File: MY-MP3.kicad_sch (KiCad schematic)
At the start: 62 parts, among them J1 microSD, J2 USB_C_Receptacle, J3 JST_2mm_LiPo, J4 Adafruit 5393 Headers, J5 Adafruit 5394 Headers, J6 Newxie Headers, J7 AudioJack4_Ground, Q1 DMG3415U, SW1 SMD_6x3.5mm_h2.5mm, U1 STM32L4R5VITx, U2 CODECODER-VS1053B_LQFP48_, U4 MAX17048, U6 MCP73831-2-OT, U7 AP7312-1833W6, Y1 ABM3-12.288MHZ-D2Y-T, Y2 8 mHz

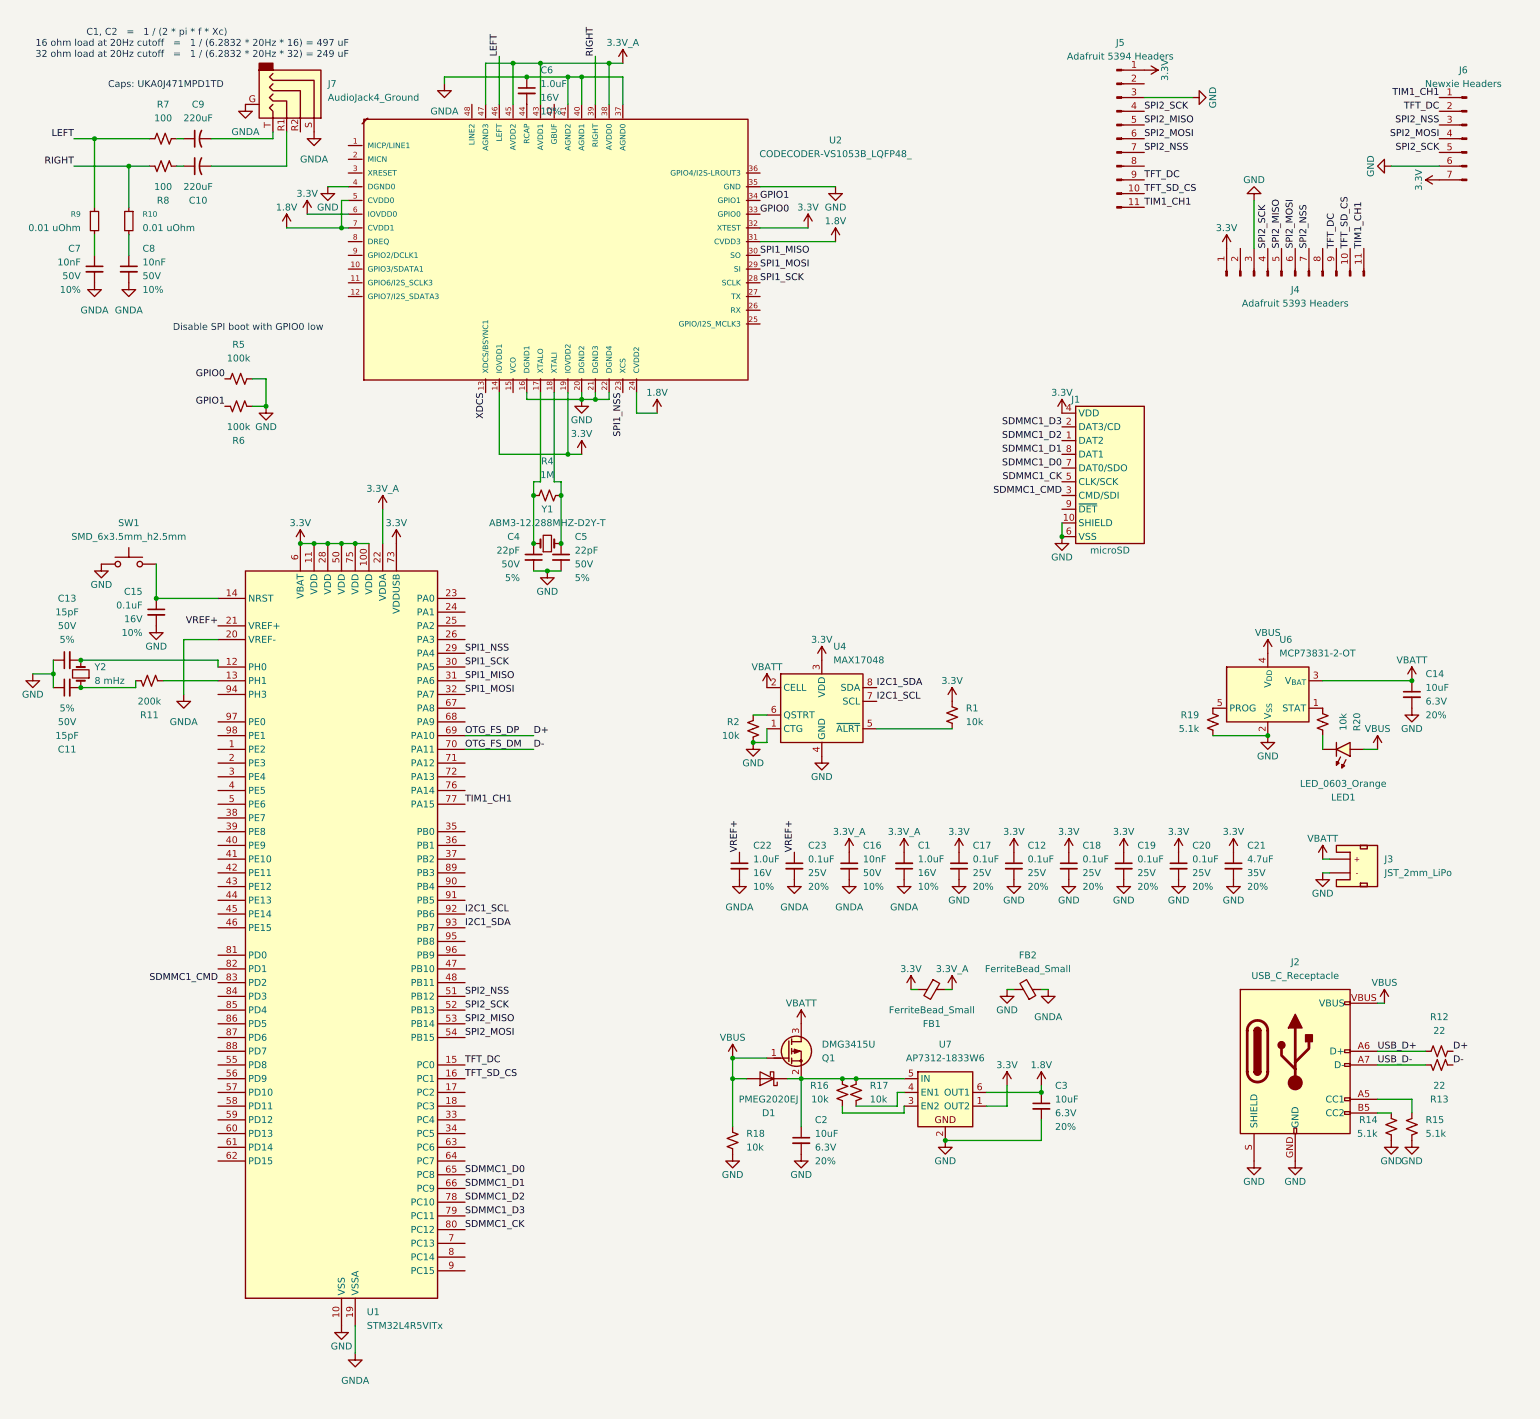
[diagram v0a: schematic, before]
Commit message: Added some buttons and started the on off hardware functionallity
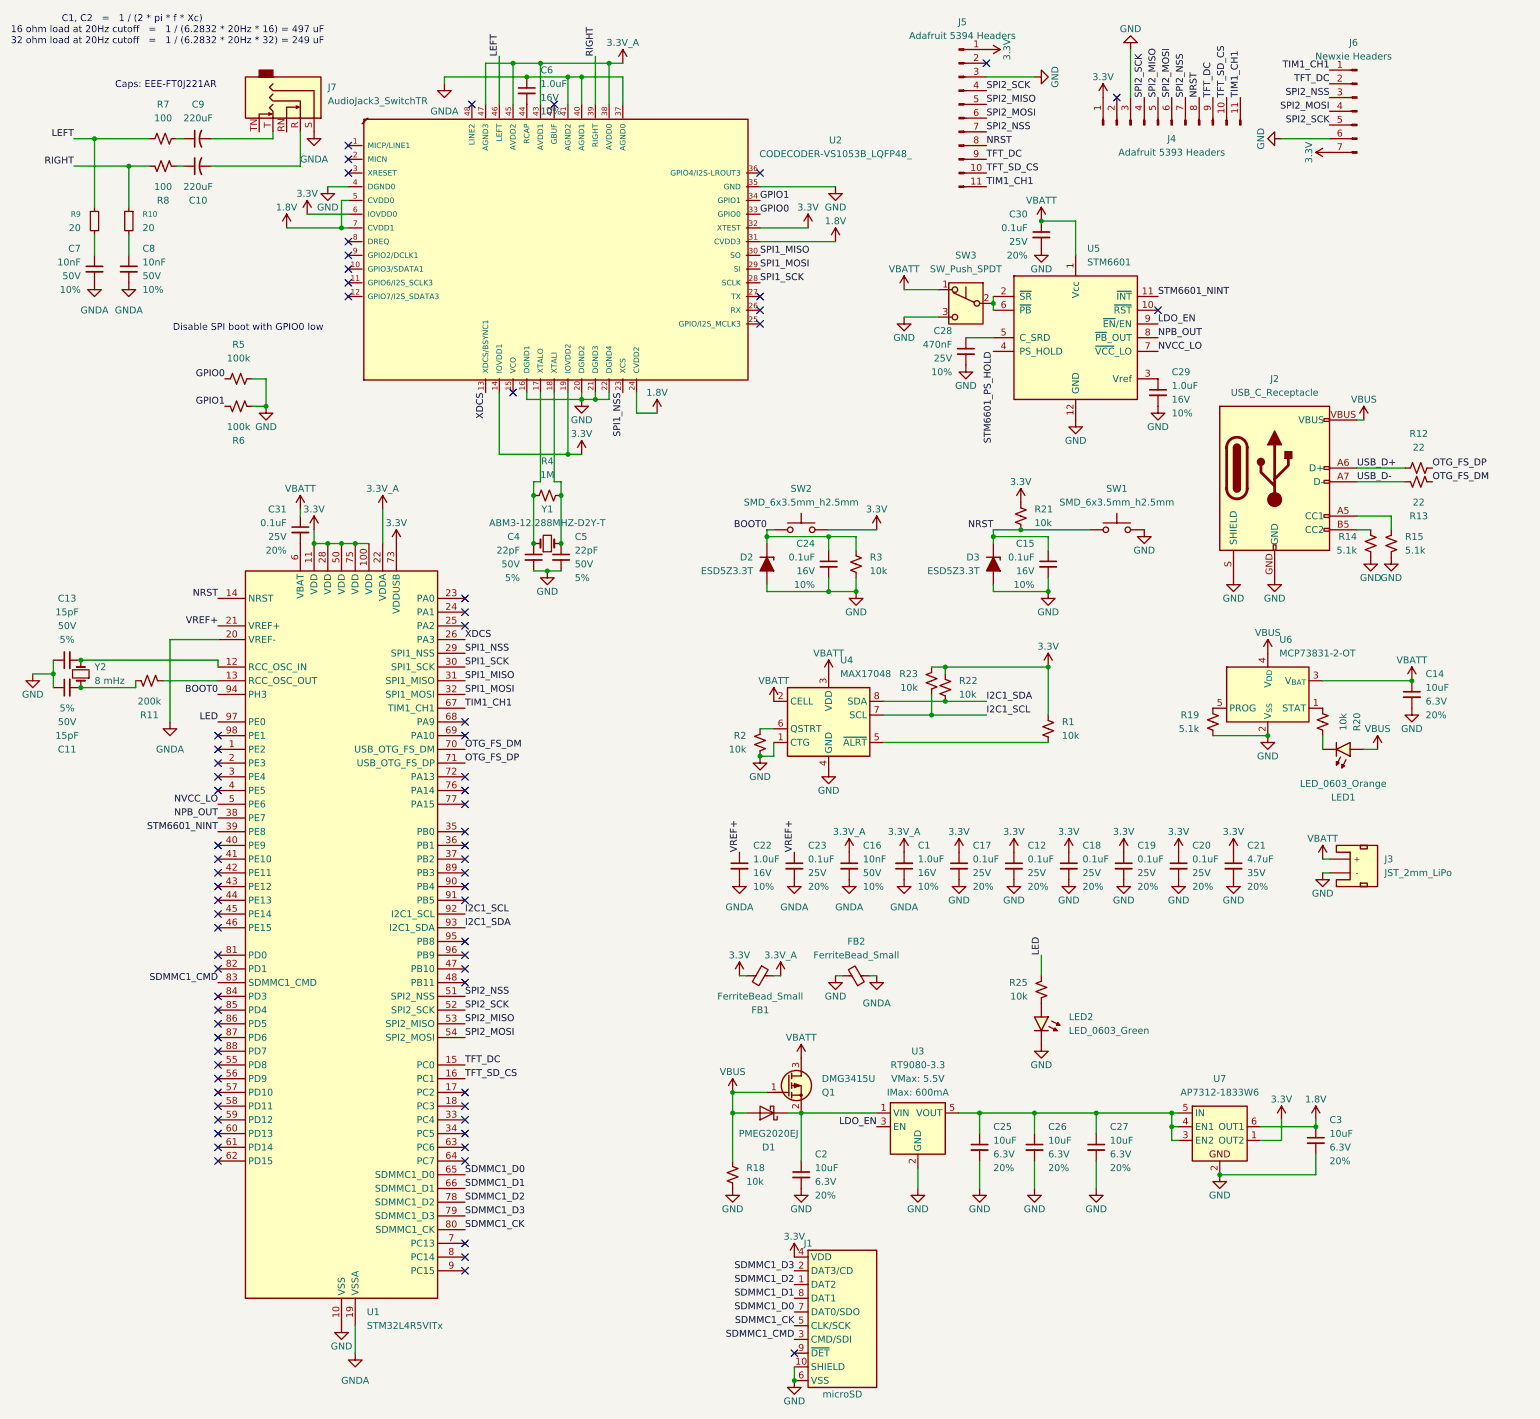
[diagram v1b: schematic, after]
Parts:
- removed J7: AudioJack4_Ground, Connector_Audio:Jack_3.5mm_CUI_SJ1-3525N_Horizontal, symbol Connector_Audio:AudioJack4_Ground
- removed R16, R17: 10k, PCM_SparkFun-Resistor:R_0603_1608Metric, symbol PCM_SparkFun-Resistor:10k_0603
- added C24: 0.1uF, PCM_SparkFun-Capacitor:C_0402_1005Metric, symbol PCM_SparkFun-Capacitor:0.1uF_0402_16V_10%
- added C25, C26, C27: 10uF, PCM_SparkFun-Capacitor:C_0603_1608Metric, symbol PCM_SparkFun-Capacitor:10uF_0603_6.3V_20%
- added C28: 470nF, PCM_SparkFun-Capacitor:C_0402_1005Metric, symbol PCM_SparkFun-Capacitor:470nF_0402_25V_10%
- added C29: 1.0uF, PCM_SparkFun-Capacitor:C_0603_1608Metric, symbol PCM_SparkFun-Capacitor:1.0uF_0603_16V_10%
- added C30, C31: 0.1uF, PCM_SparkFun-Capacitor:C_0603_1608Metric, symbol PCM_SparkFun-Capacitor:0.1uF_0603_25V_20%
- added D2, D3: ESD5Z3.3T, PCM_Diode_SMD_AKL:D_SOD-523, symbol PCM_Diode_TVS_AKL:ESD5Z3.3T
- added J7: AudioJack3_SwitchTR, Connector_Audio:Jack_3.5mm_CUI_SJ1-3525N_Horizontal, symbol Connector_Audio:AudioJack3_SwitchTR
- added LED2: LED_0603_Green, PCM_LED_SMD_AKL:LED_0603_1608Metric, symbol PCM_LED_AKL:LED_0603_Green
- added R21, R25, R3: 10k, PCM_SparkFun-Resistor:R_0603_1608Metric, symbol PCM_SparkFun-Resistor:10k_0603
- added R22, R23: 10k, PCM_SparkFun-Resistor:R_0402_1005Metric, symbol PCM_SparkFun-Resistor:10k_0402
- added SW2: SMD_6x3.5mm_h2.5mm, PCM_SparkFun-Switch:Push_SMD_6x3.5mm, symbol PCM_SparkFun-Switch:SPST_Push_SMD_6x3.5mm_h2.5mm
- added SW3: SW_Push_SPDT, symbol Switch:SW_Push_SPDT
- added U3: RT9080-3.3, PCM_SparkFun-Semiconductor-Standard:SOT23-5, symbol PCM_SparkFun-Regulator:RT9080-3.3
- added U5: STM6601, Package_DFN_QFN:TDFN-12_2x3mm_P0.5mm, symbol Power_Management:STM6601
- C10, C9: footprint (none) -> Capacitor_SMD:CP_Elec_5x5.8
- R10, R9: value 0.01 uOhm -> 20; footprint (none) -> Resistor_SMD:R_0201_0603Metric_Pad0.64x0.40mm_HandSolder
- U2: footprint CODECODER-VS1053B_LQFP48_:LQFP48-0.5-7X7MM -> Package_QFP:LQFP-48_7x7mm_P0.5mm
- Y2: footprint PCM_SparkFun-Clock:Crystal-SMD-5x3.2mm -> Crystal:Crystal_SMD_Abracon_ABM3-2Pin_5.0x3.2mm_HandSoldering
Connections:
- net 3.3V: now also R21.1, R22.2, R23.2, SW2.1; no longer U1.6 (VBAT), U4.3 (VDD)
- net GND: now also SW1.2, C24.2, C25.2, C26.2, C27.2, C28.2, C29.2, C30.2, D2.2 (A), D3.2 (A), LED2.1 (K), R3.2, SW3.3 (C), U3.2 (GND), U5.12 (GND); no longer SW1.1
- net GNDA: now also J7.S
- net I2C1_SCL: now also R23.1
- net I2C1_SDA: now also R22.1
- net TIM1_CH1: now also U1.67 (PA8); no longer U1.77 (PA15)
- net VBATT: now also U4.3 (VDD), C30.1, C31.1, SW3.1 (A), U5.1 (Vcc)
- net XDCS: now also U1.26 (PA3)
- net at C10.2: now also J7.R
- net NRST: now reaches J4.8 (Pin_8)
- net NRST: now also C15.1, J5.8 (Pin_8), SW1.1, U1.14 (NRST), D3.1 (K), R21.2
- net NPB_OUT: now reaches U1.38 (PE7)
- net NPB_OUT: now also U5.8 (~{PB}_OUT)
- net STM6601_NINT: now reaches U1.39 (PE8)
- net STM6601_NINT: now also U5.11 (~{INT})
- net NVCC_LO: now reaches U1.5 (PE6)
- net NVCC_LO: now also U5.7 (~{VCC}_LO)
- net OTG_FS_DP: now reaches U1.71 (PA12)
- net OTG_FS_DP: now also R12.2
- net BOOT0: now reaches U1.94 (PH3)
- net BOOT0: now also C24.1, D2.1 (K), R3.1, SW2.2
- net LED: now reaches U1.97 (PE0)
- net LED: now also R25.2
- net at U7.3 (EN2): now also U7.4 (EN1), U7.5 (IN), C25.1, C26.1, C27.1, U3.5 (VOUT)
- net at C2.1, D1.1 (K), Q1.2 (S): now also U3.1 (VIN); no longer U7.5 (IN)
- net at C9.2: now also J7.T
- net D+: no longer names the net of U1.69 (PA10)
- net D+: no longer R12.2
- net D- renamed OTG_FS_DM
- new net: C28.1, U5.5 (C_SRD)
- new net: LED2.2 (A), R25.1
- new net: C31.2, U1.6 (VBAT)
- new net: SW3.2 (B), U5.2 (~{SR}), U5.6 (~{PB})
- new net: C29.1, U5.3 (Vref)
- new net LDO_EN: U3.3 (EN), U5.9 (~{EN}/EN)
- new net STM6601_PS_HOLD: U5.4 (PS_HOLD)
- no-connect marks 0 -> 73
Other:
- note added: "Caps: EEE-FT0J221AR"
- note removed: "Caps: UKA0J471MPD1TD"
- moved on the sheet: C15, C2, C3, D1, FB1, FB2, J1, J2, J4, J5, J6, Q1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

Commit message: Finish Schematic and start PCB
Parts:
- removed J5: Adafruit 5394 Headers, Connector_PinSocket_2.54mm:PinSocket_1x11_P2.54mm_Vertical, symbol Connector:Conn_01x11_Pin
- removed J6: Newxie Headers, Connector_PinSocket_2.54mm:PinSocket_1x07_P2.54mm_Vertical, symbol Connector:Conn_01x07_Pin
- removed SW3: SW_Push_SPDT, symbol Switch:SW_Push_SPDT
- added J9: Conn_01x04_FPC, Connector_FFC-FPC:Amphenol_F32Q-1A7x1-11004_1x04-1MP_P0.5mm_Horizontal, symbol Connector_Generic_MountingPin:Conn_01x04_MountingPin
- added LED3: LED_0603_Red, PCM_LED_SMD_AKL:LED_0603_1608Metric, symbol PCM_LED_AKL:LED_0603_Red
- added R16: 10k, PCM_SparkFun-Resistor:R_0603_1608Metric, symbol PCM_SparkFun-Resistor:10k_0603
- added SW3: BTN_POW, PCM_SparkFun-Switch:Push_SMD_RA_4.5x3.4mm, symbol PCM_SparkFun-Switch:SPST_Push_SMD_RA_4.5x3.4mm_h3.3mm
- added SW4: BTN_VUP, PCM_SparkFun-Switch:Push_SMD_RA_4.5x3.4mm, symbol PCM_SparkFun-Switch:SPST_Push_SMD_RA_4.5x3.4mm_h3.3mm
- added SW5: BTN_VDN, PCM_SparkFun-Switch:Push_SMD_RA_4.5x3.4mm, symbol PCM_SparkFun-Switch:SPST_Push_SMD_RA_4.5x3.4mm_h3.3mm
- added SW6: Nav Switch, PCM_SparkFun-Switch:Navigation_SMD_9.9x9.9mm, symbol PCM_SparkFun-Switch:Navigation_5Way_SMD_9.9x9.9mm
- added SW7: BTN_OPT, PCM_SparkFun-Switch:Push_SMD_6x3.5mm, symbol PCM_SparkFun-Switch:SPST_Push_SMD_6x3.5mm_h2.5mm
- added SW8: BTN_SEL, PCM_SparkFun-Switch:Push_SMD_6x3.5mm, symbol PCM_SparkFun-Switch:SPST_Push_SMD_6x3.5mm_h2.5mm
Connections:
- net 3.3V_A: now also J9.2 (Pin_2)
- net GND: now also SW3.1, SW4.2, SW5.2, SW6.10 (GND), SW6.3 (GND), SW6.6 (GND), SW6.8 (GND), SW6.9 (GND), SW7.2, SW8.2
- net GNDA: now also J9.4 (Pin_4), J9.MP (MountPin)
- net NVCC_LO: now also LED3.1 (K)
- net TFT_DC: now also U1.17 (PC2); no longer U1.15 (PC0)
- net TFT_SD_CS: now also U1.18 (PC3); no longer U1.16 (PC1)
- net VBATT: now also R16.2
- net BTN_OPT: now reaches U1.55 (PD8)
- net BTN_OPT: now also SW7.1
- net BTN_SEL: now reaches U1.56 (PD9)
- net BTN_SEL: now also SW8.1
- net BTN_PLAY: now reaches U1.57 (PD10)
- net BTN_PLAY: now also SW6.4 (Center)
- net BTN_UP: now reaches U1.58 (PD11)
- net BTN_UP: now also SW6.1 (Up)
- net BTN_DN: now reaches U1.59 (PD12)
- net BTN_DN: now also SW6.5 (Down)
- net BTN_TRACK: now reaches U1.60 (PD13)
- net BTN_TRACK: now also SW6.7 (Left)
- net BTN_SEEK: now reaches U1.61 (PD14)
- net BTN_SEEK: now also SW6.2 (Right)
- net BTN_VUP: now reaches U1.87 (PD6)
- net BTN_VUP: now also SW4.1
- net BTN_VDN: now reaches U1.88 (PD7)
- net BTN_VDN: now also SW5.1
- net at U5.2 (~{SR}), U5.6 (~{PB}): now also SW3.2
- new net: LED3.2 (A), R16.1
- new net JOY_X: J9.1 (Pin_1), U1.15 (PC0)
- new net JOY_Y: J9.3 (Pin_3), U1.16 (PC1)
- no-connect marks 73 -> 61
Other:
- moved on the sheet: C15, C24, C28, C29, C30, D2, D3, J4, LED2, R21, R25, R3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

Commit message: Redo PCB for smaller size and better bin placements
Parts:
- removed J9: Conn_01x04_FPC, Connector_FFC-FPC:Amphenol_F32Q-1A7x1-11004_1x04-1MP_P0.5mm_Horizontal, symbol Connector_Generic_MountingPin:Conn_01x04_MountingPin
- C1, C11, C12, C13, C14, C16, C17, C18, C19, C2, C20, C21, C22, C23, C25, C26, C27, C29, C3, C30, C31, C6: footprint PCM_SparkFun-Capacitor:C_0603_1608Metric -> PCM_Capacitor_SMD_Handsoldering_AKL:C_0402_1005Metric_Pad0.74x0.62mm
- C15, C24, C28, C4, C5, C7, C8: footprint PCM_SparkFun-Capacitor:C_0402_1005Metric -> PCM_Capacitor_SMD_Handsoldering_AKL:C_0402_1005Metric_Pad0.74x0.62mm
- FB1, FB2: footprint Inductor_SMD:L_0603_1608Metric_Pad1.05x0.95mm_HandSolder -> Inductor_SMD:L_0402_1005Metric_Pad0.77x0.64mm_HandSolder
- LED1: footprint PCM_LED_SMD_AKL:LED_0603_1608Metric -> PCM_SparkFun-LED:LED_0402_1005Metric_Orange
- LED2: footprint PCM_LED_SMD_AKL:LED_0603_1608Metric -> PCM_SparkFun-LED:LED_0402_1005Metric_Green
- LED3: footprint PCM_LED_SMD_AKL:LED_0603_1608Metric -> PCM_SparkFun-LED:LED_0402_1005Metric_Red
- R11, R12, R13, R14, R15, R16, R18, R19, R20, R21, R25, R3, R4, R5, R6, R7, R8: footprint PCM_SparkFun-Resistor:R_0603_1608Metric -> PCM_SparkFun-Resistor:R_0402_1005Metric
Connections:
- net JOY_X is gone; now on net BTN_PLAY: U1.15 (PC0)
- net JOY_Y is gone; now on net BTN_UP: U1.16 (PC1)
- net BTN_DN: now also U1.17 (PC2); no longer U1.59 (PD12)
- net BTN_OPT: now also U1.8 (PC14); no longer U1.55 (PD8)
- net BTN_PLAY: no longer U1.57 (PD10)
- net BTN_SEEK: now also U1.23 (PA0); no longer U1.61 (PD14)
- net BTN_SEL: now also U1.9 (PC15); no longer U1.56 (PD9)
- net BTN_TRACK: now also U1.18 (PC3); no longer U1.60 (PD13)
- net BTN_UP: no longer U1.58 (PD11)
- net BTN_VDN: now also U1.7 (PC13); no longer U1.88 (PD7)
- net BTN_VUP: now also U1.5 (PE6); no longer U1.87 (PD6)
- net LED: now also U1.1 (PE2); no longer U1.97 (PE0)
- net NPB_OUT: now also U1.3 (PE4); no longer U1.38 (PE7)
- net NVCC_LO: now also U1.2 (PE3); no longer U1.5 (PE6)
- net SPI1_MISO: now also J4.5 (Pin_5); no longer U2.30 (SO)
- net SPI1_MOSI: now also J4.6 (Pin_6); no longer U2.29 (SI)
- net SPI1_NSS: now also J4.7 (Pin_7); no longer U2.23 (XCS)
- net SPI1_SCK: now also J4.4 (Pin_4); no longer U2.28 (SCLK)
- net SPI2_MISO: now also U2.30 (SO); no longer J4.5 (Pin_5)
- net SPI2_MOSI: now also U2.29 (SI); no longer J4.6 (Pin_6)
- net SPI2_NSS: now also U2.23 (XCS); no longer J4.7 (Pin_7)
- net SPI2_SCK: now also U2.28 (SCLK); no longer J4.4 (Pin_4)
- net STM6601_NINT: now also U1.4 (PE5); no longer U1.39 (PE8)
- net TFT_DC: now also U1.33 (PC4); no longer U1.17 (PC2)
- net TFT_SD_CS: now also U1.34 (PC5); no longer U1.18 (PC3)
- net TIM1_CH1: now also U1.40 (PE9); no longer U1.67 (PA8)
- net XDCS: now also U1.63 (PC6); no longer U1.26 (PA3)
- no-connect marks 61 -> 63
